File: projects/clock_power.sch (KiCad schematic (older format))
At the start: 6 parts, among them U201 LT1761

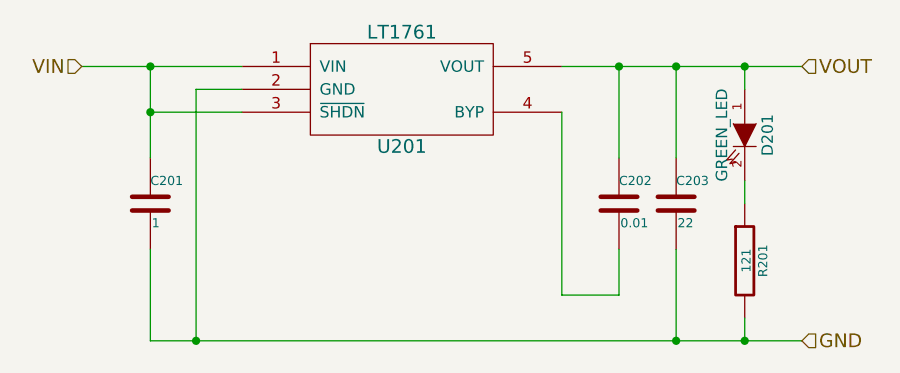
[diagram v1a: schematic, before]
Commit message: add box cap and small electrolytic cap footprints
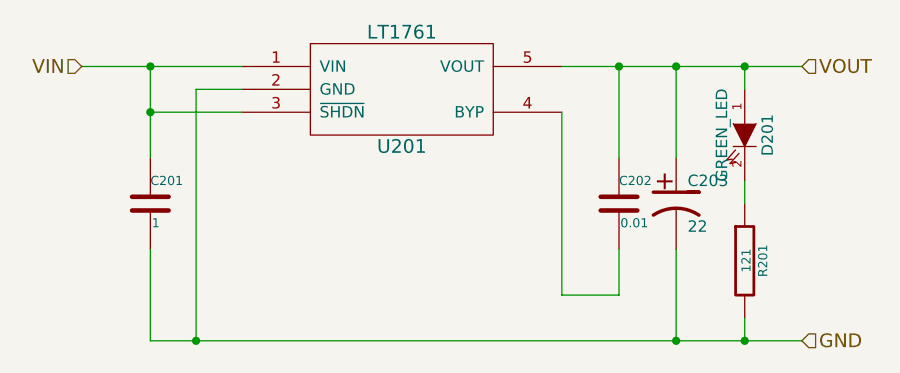
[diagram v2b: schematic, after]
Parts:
- removed C203: 22, symbol C
- added C203: 22, symbol CP1
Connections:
- net GND: now also C203.2
- net VOUT: now also C203.1
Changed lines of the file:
@@
 VOUT
-$Comp
-L C C203
-U 1 1 544A157E
-P 6900 4400
-F 0 "C203" H 6900 4500 40  0000 L CNN
-F 1 "22" H 6906 4315 40  0000 L CNN
-F 2 "" H 6938 4250 30  0000 C CNN
-F 3 "" H 6900 4400 60  0000 C CNN
-F 4 "Digi-Key" H 6900 4400 60  0001 C CNN "Supplier"
-F 5 "P16405CT-ND" H 6900 4400 60  0001 C CNN "Supplier-PN"
-F 6 "Panasonic" H 6900 4400 60  0001 C CNN "Manu"
-F 7 "32SEPF22M+TSS" H 6900 4400 60  0001 C CNN "Manu-PN"
-F 8 "CAP ALUM 22UF 32V 20% RADIAL" H 6900 4400 60  0001 C CNN "Description"
-	1    6900 4400
-	1    0    0    -1
-$EndComp
 $Comp
 L C C202
@@
 	5000 4000 4600 4000
 Connection ~ 4600 4000
+$Comp
+L CP1 C203
+U 1 1 54858D85
+P 6900 4400
+F 0 "C203" H 6950 4500 50  0000 L CNN
+F 1 "22" H 6950 4300 50  0000 L CNN
+F 2 "" H 6900 4400 60  0000 C CNN
+F 3 "" H 6900 4400 60  0000 C CNN
+F 4 "Digi-key" H 6900 4400 60  0001 C CNN "Supplier"
+F 5 "P16405CT-ND" H 6900 4400 60  0001 C CNN "Supplier-PN"
+F 6 "Panasonic" H 6900 4400 60  0001 C CNN "Manu"
+F 7 "32SEPF22M+TSS" H 6900 4400 60  0001 C CNN "Manu-PN"
+F 8 "CAP ALUM 22UF 32V 20% RADIAL" H 6900 4400 60  0001 C CNN "Description"
+	1    6900 4400
+	1    0    0    -1
+$EndComp
 $EndSCHEMATC
